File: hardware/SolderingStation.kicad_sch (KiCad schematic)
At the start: 15 parts, among them U1 MCP6002-xSN, U2 ADS1115

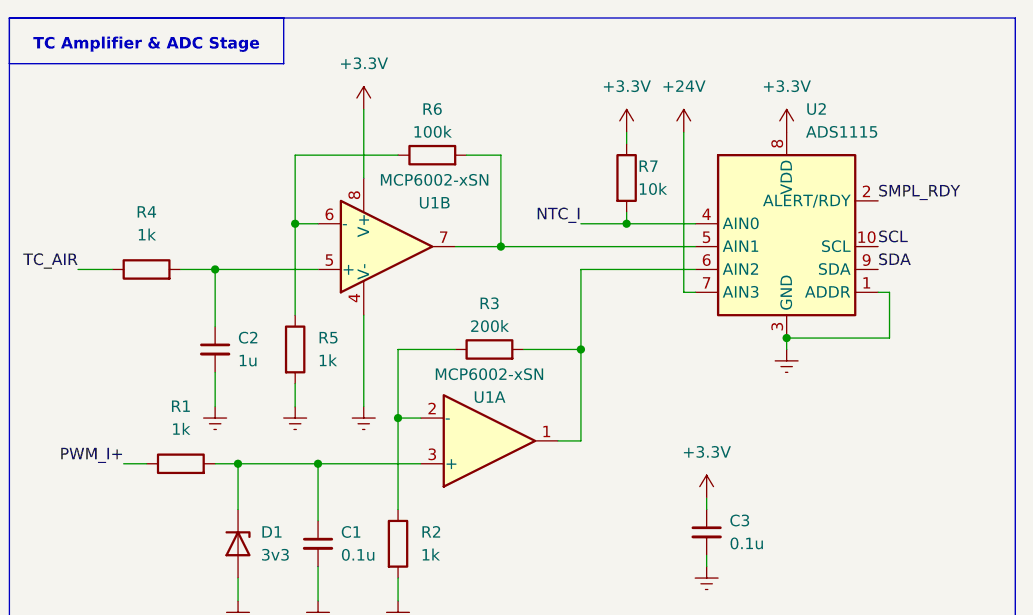
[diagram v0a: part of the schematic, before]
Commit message: fix: ADC
24V converting fix
PWD_I resistor fix
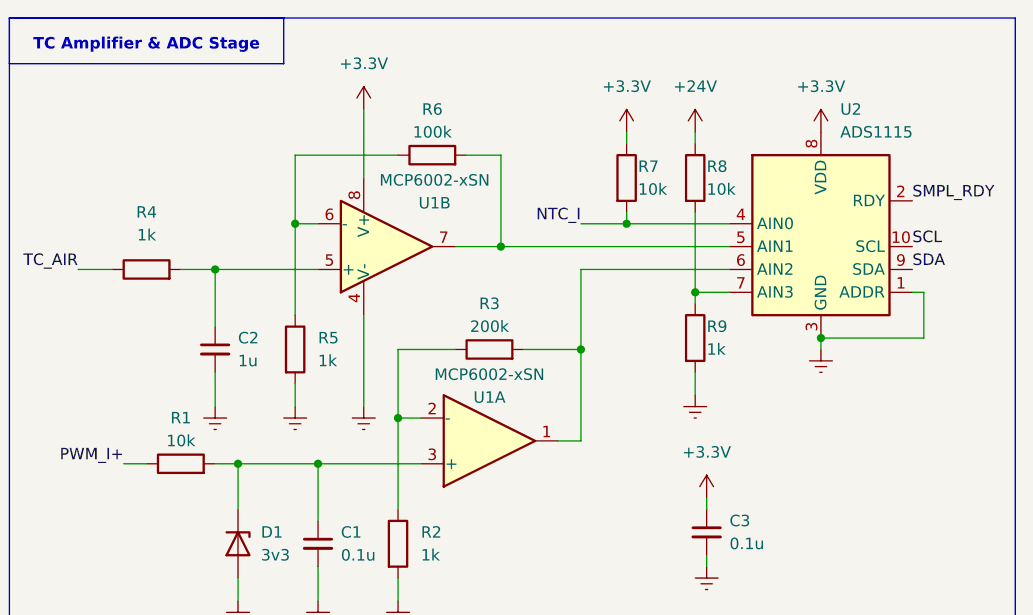
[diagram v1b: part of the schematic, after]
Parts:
- added R8: 10k, symbol Device:R
- added R9: 1k, symbol Device:R
- R1: value 1k -> 10k
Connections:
- net +24V: now also R8.1; no longer U2.7 (AIN3)
- net GNDREF: now also R9.2
- new net: R8.2, R9.1, U2.7 (AIN3)
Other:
- moved on the sheet: U2

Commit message: feature: heater switch
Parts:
- added C4: 10u 35V, symbol Device:C_Small
- added D2: SS54, Diode_THT:D_DO-35_SOD27_P2.54mm_Vertical_KathodeUp, symbol Diode:B160-E3
- added D3: 1N4715A, Diode_THT:D_DO-41_SOD81_P10.16mm_Horizontal, symbol Diode:1N47xxA
- added Q1: IRLZ44N, Package_TO_SOT_THT:TO-220-3_Vertical, symbol SolderingStationLib:IRLZ44N
- added Q2: S8050, Package_TO_SOT_THT:TO-92_Inline, symbol Transistor_BJT:S8050
- added R10: 1k, symbol Device:R
- added R11: 10k, symbol Device:R
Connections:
- net +24V: now also D2.2 (A), Q1.2 (D)
- net GNDREF: now also Q2.1 (E)
- new net: Q2.2 (B), R11.2
- new net: D3.1 (K), Q1.1 (G), Q2.3 (C), R10.2
- new net: C4.1, D2.1 (K), R10.1
- new net PWD_CTRL: R11.1
- new net PWD_I+: C4.2, D3.2 (A), Q1.3 (S)
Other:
- note added: "Heater Hight side switch"

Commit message: feature: fan logic
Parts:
- added J1: AC Screw Terminal, symbol Connector:Screw_Terminal_01x03
- added Q3: BTA16-600B, Package_TO_SOT_THT:TO-220-3_Vertical, symbol Triac_Thyristor:BTA16-600B
- added R12: 300, symbol Device:R
- added R13, R14: 390/0.5W, symbol Device:R
- added U3: MOC3063M, symbol Relay_SolidState:MOC3063M
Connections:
- net COIL: now also Q3.1 (A1), R14.2
- net GNDREF: now also U3.2
- net PE: now also J1.3 (Pin_3)
- net COIL_ renamed NEUTRAL
- net PWD_A+ renamed PWM_A+
- net PWD_A- renamed PWM_A-
- new net: R12.2, U3.1
- new net: Q3.3 (G), R14.1, U3.4
- new net: R13.1, U3.6
- new net CD: R12.1
- new net Neutral: J1.2 (Pin_2)
- new net ~220: J1.1 (Pin_1), Q3.2 (A2), R13.2
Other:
- note added: "COIL DIMMER"
- note added: "Connectors Pinout"
- note removed: "Iron & Hot Air Pinout"

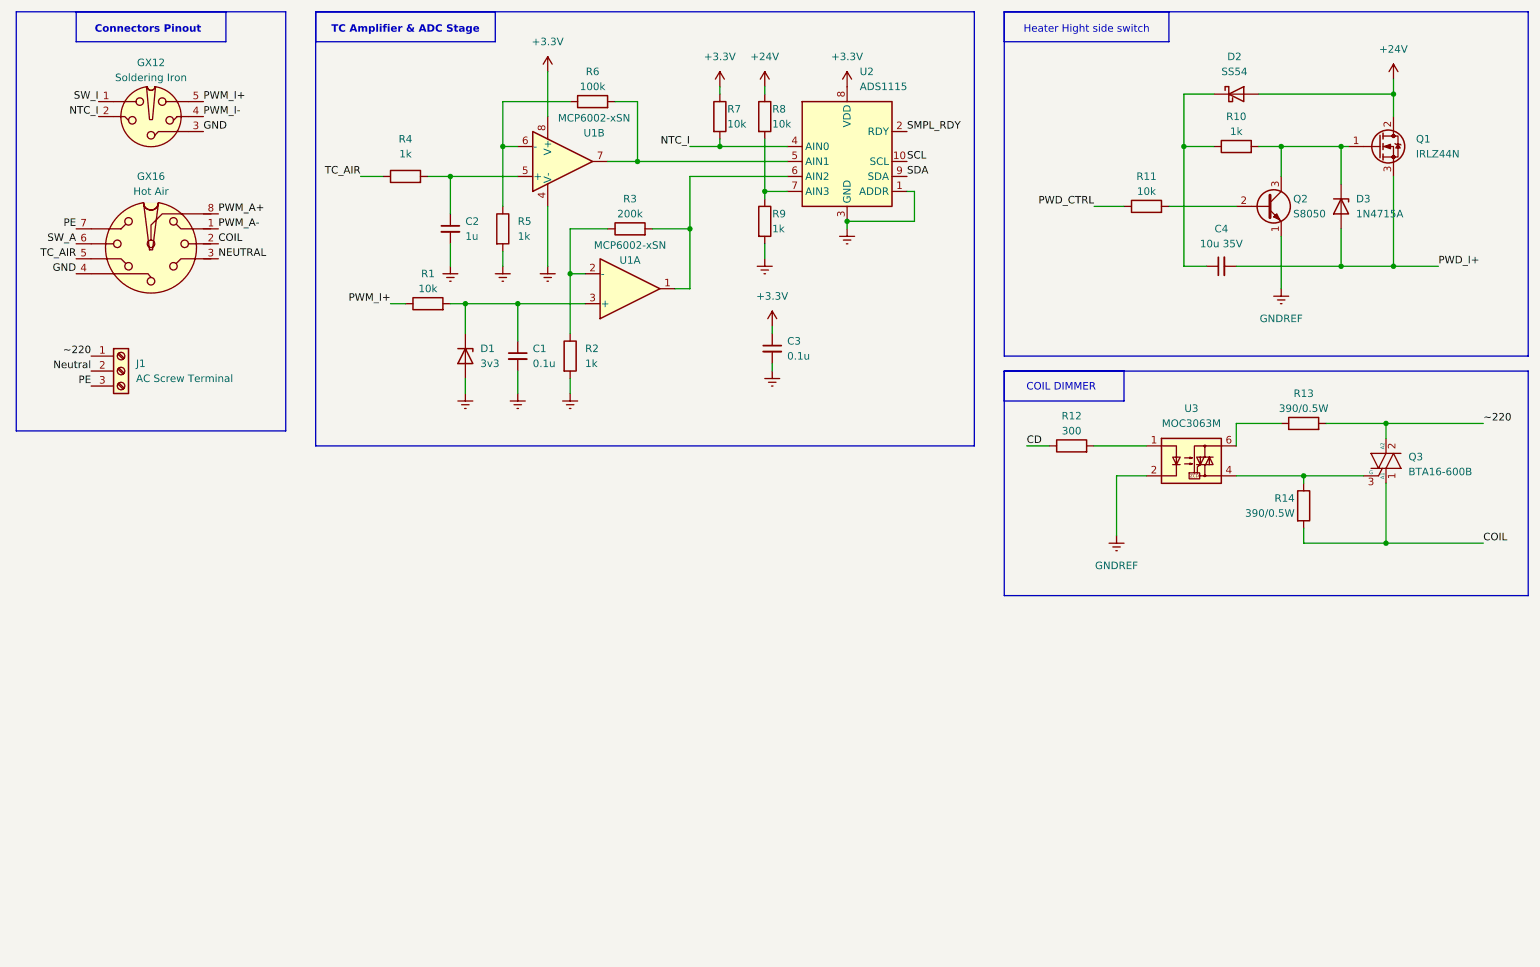
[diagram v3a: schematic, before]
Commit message: feature: basic nodes
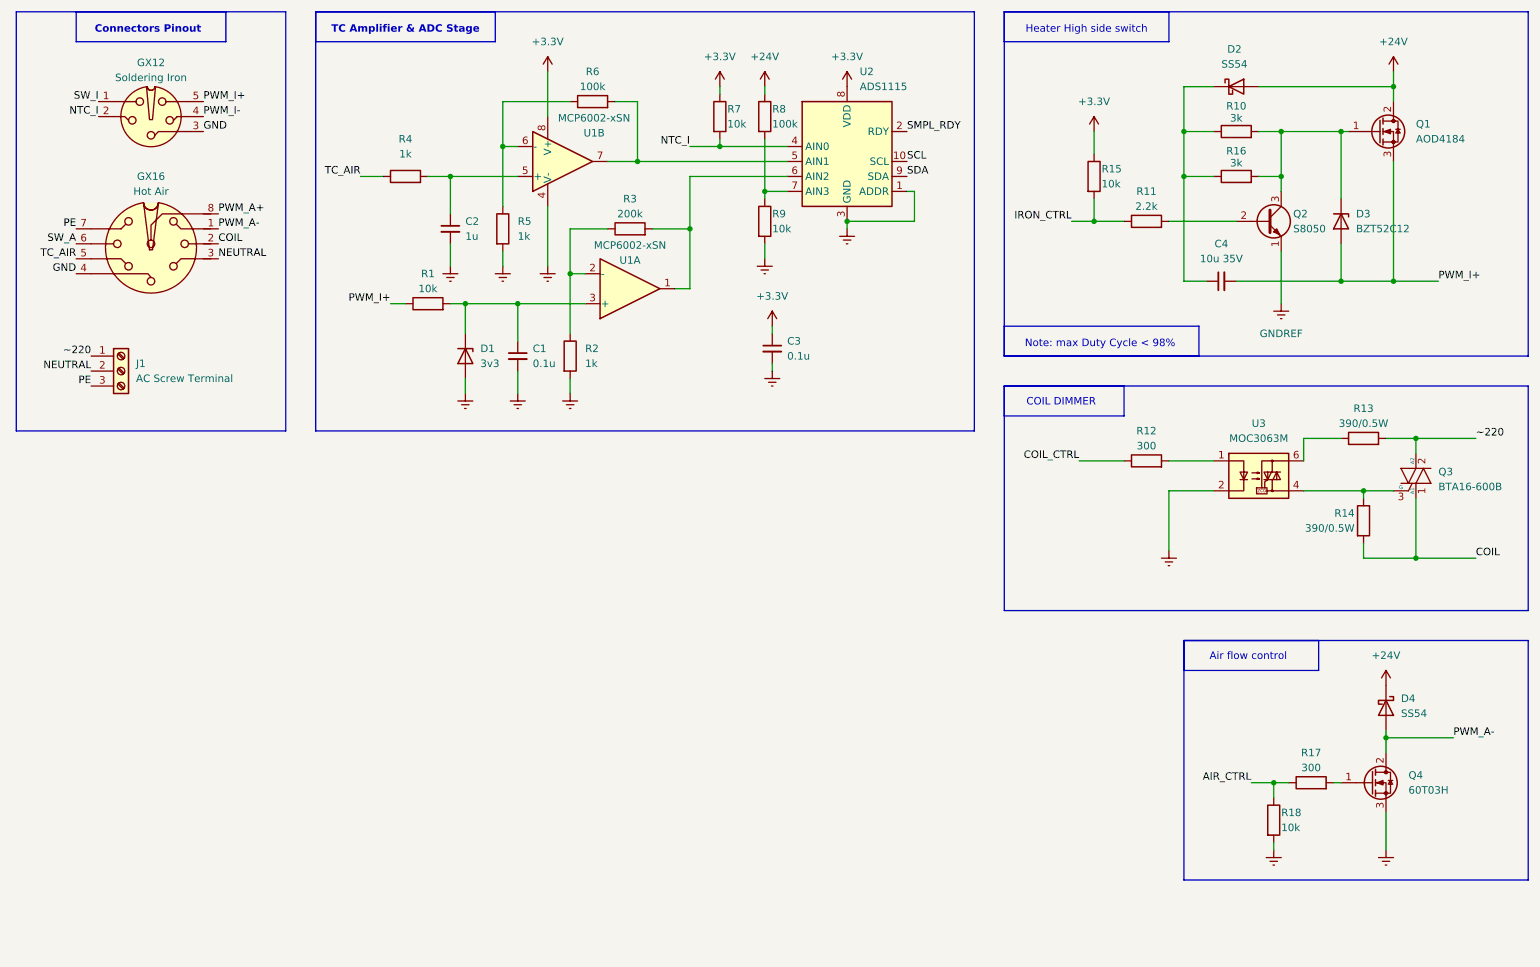
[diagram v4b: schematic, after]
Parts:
- removed D3: 1N4715A, Diode_THT:D_DO-41_SOD81_P10.16mm_Horizontal, symbol Diode:1N47xxA
- removed Q1: IRLZ44N, Package_TO_SOT_THT:TO-220-3_Vertical, symbol SolderingStationLib:IRLZ44N
- added D3: BZT52C12, Diode_SMD:D_SOD-123F, symbol Diode:BZT52Bxx
- added D4: SS54, Diode_THT:D_DO-35_SOD27_P2.54mm_Vertical_KathodeUp, symbol Diode:B160-E3
- added Q1: AOD4184, symbol Transistor_FET:Q_NMOS_GDS
- added Q4: 60T03H, symbol SolderingStationLib:60T03H
- added R15, R18: 10k, symbol Device:R
- added R16: 3k, symbol Device:R
- added R17: 300, symbol Device:R
- R10: value 1k -> 3k
- R11: value 10k -> 2.2k
- R8: value 10k -> 100k
- R9: value 1k -> 10k
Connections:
- net Neutral is gone; now on net NEUTRAL: J1.2 (Pin_2)
- net PWD_I+ is gone; now on net PWM_I+: C4.2
- net +24V: now also D4.1 (K), Q1.2 (D)
- net +3.3V: now also R15.1
- net GNDREF: now also Q4.3 (S), R18.2
- net PWM_A-: now also D4.2 (A), Q4.2 (D)
- net PWM_I+: now also D3.2 (A), Q1.3 (S)
- net at Q2.3 (C), R10.2: now also D3.1 (K), Q1.1 (G), R16.2
- net at C4.1, D2.1 (K), R10.1: now also R16.1
- net CD renamed COIL_CTRL
- net PWD_CTRL renamed IRON_CTRL
- net IRON_CTRL: now also R15.2
- new net: Q4.1 (G), R17.2
- new net AIR_CTRL: R17.1, R18.1
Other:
- note added: "Air flow control"
- note added: "Heater High side switch"
- note added: "Note: max Duty Cycle < 98%"
- note removed: "Heater Hight side switch"
- moved on the sheet: C4, D2, Q2, Q3, R10, R11, R12, R13, R14, U3

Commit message: peripherals done
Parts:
- removed C1, C3: 0.1u, symbol Device:C_Small
- removed C2: 1u, symbol Device:C_Small
- removed C4: 10u 35V, symbol Device:C_Small
- removed D1: 3v3, symbol Device:D_Zener
- removed D2, D4: SS54, Diode_THT:D_DO-35_SOD27_P2.54mm_Vertical_KathodeUp, symbol Diode:B160-E3
- removed D3: BZT52C12, Diode_SMD:D_SOD-123F, symbol Diode:BZT52Bxx
- removed Q1: AOD4184, symbol Transistor_FET:Q_NMOS_GDS
- removed Q2: S8050, Package_TO_SOT_THT:TO-92_Inline, symbol Transistor_BJT:S8050
- removed Q3: BTA16-600B, Package_TO_SOT_THT:TO-220-3_Vertical, symbol Triac_Thyristor:BTA16-600B
- removed Q4: 60T03H, symbol SolderingStationLib:60T03H
- removed R1, R15, R18, R7, R9: 10k, symbol Device:R
- removed R10, R16: 3k, symbol Device:R
- removed R11: 2.2k, symbol Device:R
- removed R12, R17: 300, symbol Device:R
- removed R13, R14: 390/0.5W, symbol Device:R
- removed R2, R4, R5: 1k, symbol Device:R
- removed R3: 200k, symbol Device:R
- removed R6, R8: 100k, symbol Device:R
- removed U1: MCP6002-xSN, symbol SolderingStationLib:MCP6002-xSN
- removed U2: ADS1115, Package_SO:TSSOP-10_3x3mm_P0.5mm, symbol SolderingStationLib:ADS1115
- removed U3: MOC3063M, symbol Relay_SolidState:MOC3063M
- added J2: Iron Encoder, symbol Connector_Generic:Conn_01x05
- added J3: Hot Air Encoder, symbol Connector_Generic:Conn_01x05
- added J4: OLED, symbol Connector_Generic:Conn_01x04
- added J5: STM32 SWD, symbol Connector_Generic:Conn_01x04
- added J6: ESP UART, symbol Connector_Generic:Conn_01x04
- added J7: STM BOOT, symbol Connector_Generic:Conn_01x03
- added J8: +5V, symbol Connector:Screw_Terminal_01x02
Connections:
- net +3.3V: now also J2.1 (Pin_1), J3.1 (Pin_1), J4.2 (Pin_2)
- net GND: now also J2.5 (Pin_5), J3.5 (Pin_5), J4.1 (Pin_1), J5.4 (Pin_4), J6.2 (Pin_2), J7.3 (Pin_3), J8.2 (Pin_2)
- net SCL: now also J4.3 (Pin_3)
- net SDA: now also J4.4 (Pin_4)
- new net +5V: J8.1 (Pin_1)
- new net 3.3V: J6.1 (Pin_1)
- new net 3.3V_SWD: J5.1 (Pin_1)
- new net 3V3_STM: J7.1 (Pin_1)
- new net AE_KEY: J3.2 (Pin_2)
- new net AE_S1: J3.4 (Pin_4)
- new net AE_S2: J3.3 (Pin_3)
- new net BOOT_STM: J7.2 (Pin_2)
- new net IE_KEY: J2.2 (Pin_2)
- new net IE_S1: J2.4 (Pin_4)
- new net IE_S2: J2.3 (Pin_3)
- new net RX_ESP: J6.4 (Pin_4)
- new net SWDCLK: J5.3 (Pin_3)
- new net SWDIO: J5.2 (Pin_2)
- new net TX_ESP: J6.3 (Pin_3)
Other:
- added sheet AirHeater (airHeater.kicad_sch)
- added sheet Heater High side switch (heaterSwitch.kicad_sch)
- added sheet Main Unit (MUG.kicad_sch)
- added sheet TC Amplifier & ADC Stage (ADC.kicad_sch)
- note removed: "Air flow control"
- note removed: "COIL DIMMER"
- note removed: "Heater High side switch"
- note removed: "Note: max Duty Cycle < 98%"
- note removed: "TC Amplifier & ADC Stage"

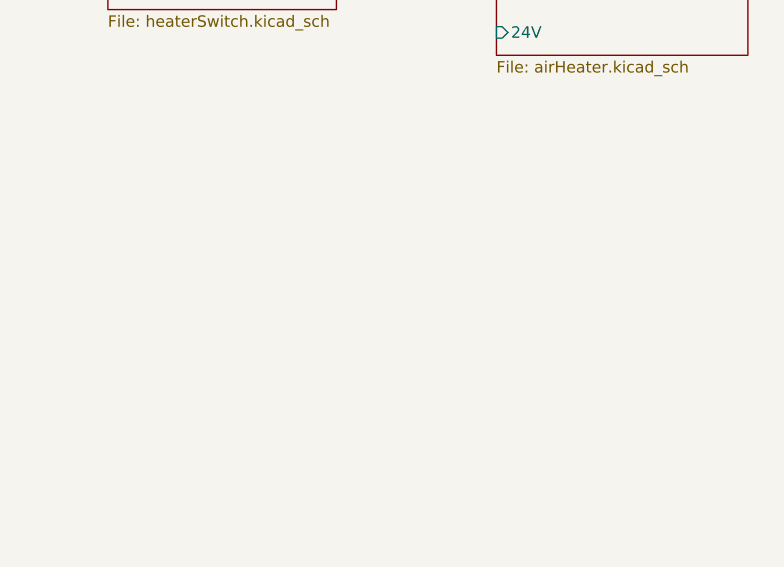
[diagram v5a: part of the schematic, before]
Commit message: feature: safety relay
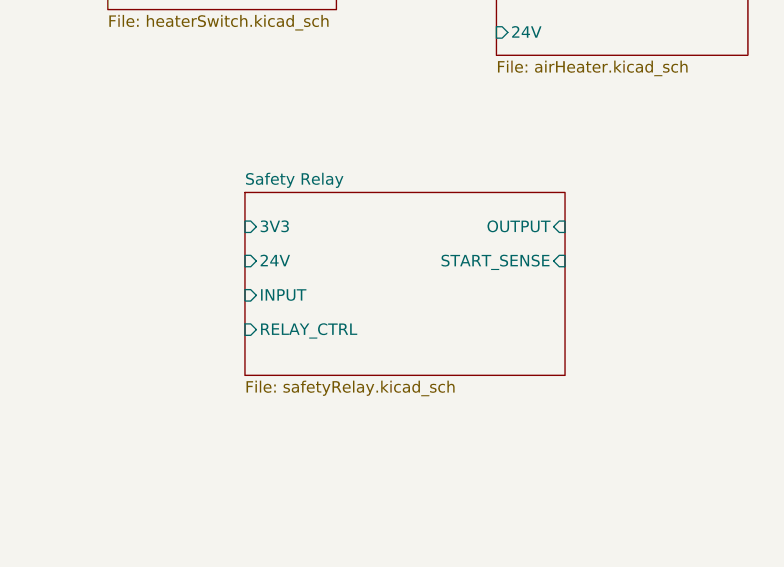
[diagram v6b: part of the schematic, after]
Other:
- added sheet Safety Relay (safetyRelay.kicad_sch)
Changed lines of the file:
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@@
+		)
+	)
+	(sheet
+		(at 170.18 71.12)
+		(size 35.56 20.32)
+		(exclude_from_sim no)
+		(in_bom yes)
+		(on_board yes)
+		(dnp no)
+		(fields_autoplaced yes)
+		(stroke
+			(width 0.1524)
+			(type solid)
+		)
+		(fill
+			(color 0 0 0 0.0000)
+		)
+		(property "Sheetname" "Safety Relay"
+			(at 170.18 70.4084 0)
+			(effects
+				(font
+					(size 1.27 1.27)
+				)
+				(justify left bottom)
+			)
+		)
+		(property "Sheetfile" "safetyRelay.kicad_sch"
+			(at 170.18 92.0246 0)
+			(effects
+				(font
+					(size 1.27 1.27)
+				)
+				(justify left top)
+			)
+		)
+		(pin "3V3" input
+			(at 170.18 74.93 180)
+			(effects
+				(font
+					(size 1.27 1.27)
+				)
+				(justify left)
+			)
+		)
+		(pin "24V" input
+			(at 170.18 78.74 180)
+			(effects
+				(font
+					(size 1.27 1.27)
+				)
+				(justify left)
+			)
+		)
+		(pin "INPUT" input
+			(at 170.18 82.55 180)
+			(effects
+				(font
+					(size 1.27 1.27)
+				)
+				(justify left)
+			)
+		)
+		(pin "OUTPUT" input
+			(at 205.74 74.93 0)
+			(effects
+				(font
+					(size 1.27 1.27)
+				)
+				(justify right)
+			)
+		)
+		(pin "RELAY_CTRL" input
+			(at 170.18 86.36 180)
+			(effects
+				(font
+					(size 1.27 1.27)
+				)
+				(justify left)
+			)
+		)
+		(pin "START_SENSE" input
+			(at 205.74 78.74 0)
+			(effects
+				(font
+					(size 1.27 1.27)
+				)
+				(justify right)
+			)
+		)
+		(instances
+			(project "SolderingStation"
+				(path "/23f2f192-8d8a-4d18-9a9e-f5d6a1224b2d"
+					(page "6")
+				)
+			)
 		)
 	)
